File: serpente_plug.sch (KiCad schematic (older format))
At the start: 26 parts, among them J1 USB_A, J2 Conn_Power, J3 Conn_GPIO, SW1 SW_RESET, U1 GD25Q32CNIGR, U2 MCP1700-3302E_SOT23, U3 ATSAMD21E18A

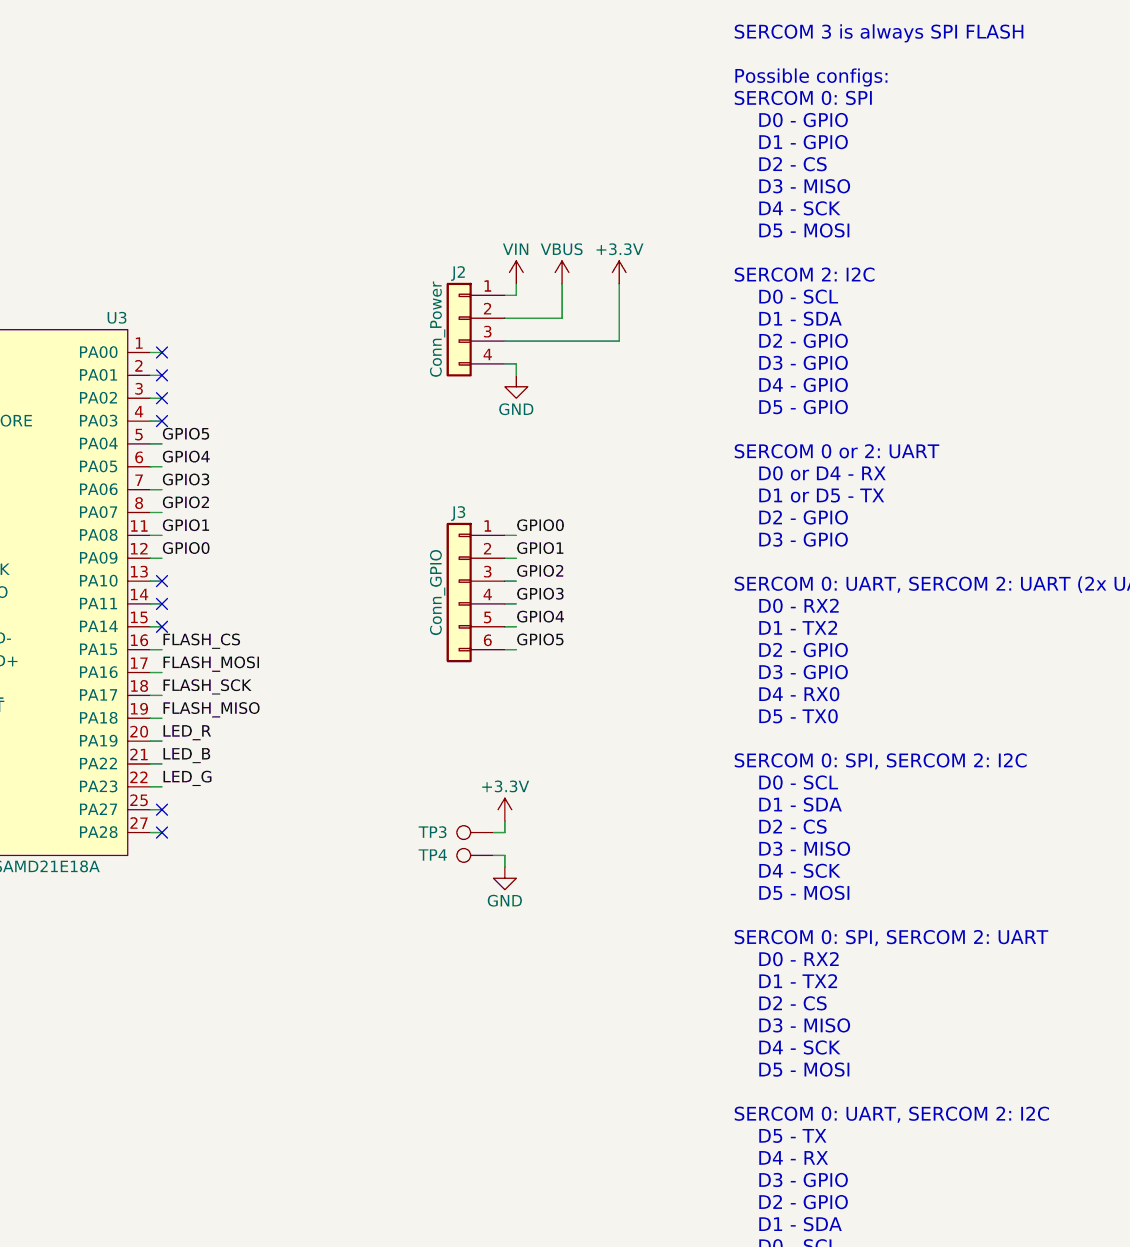
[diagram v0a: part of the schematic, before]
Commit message: Fix GPIO numbers, add BOM, update README
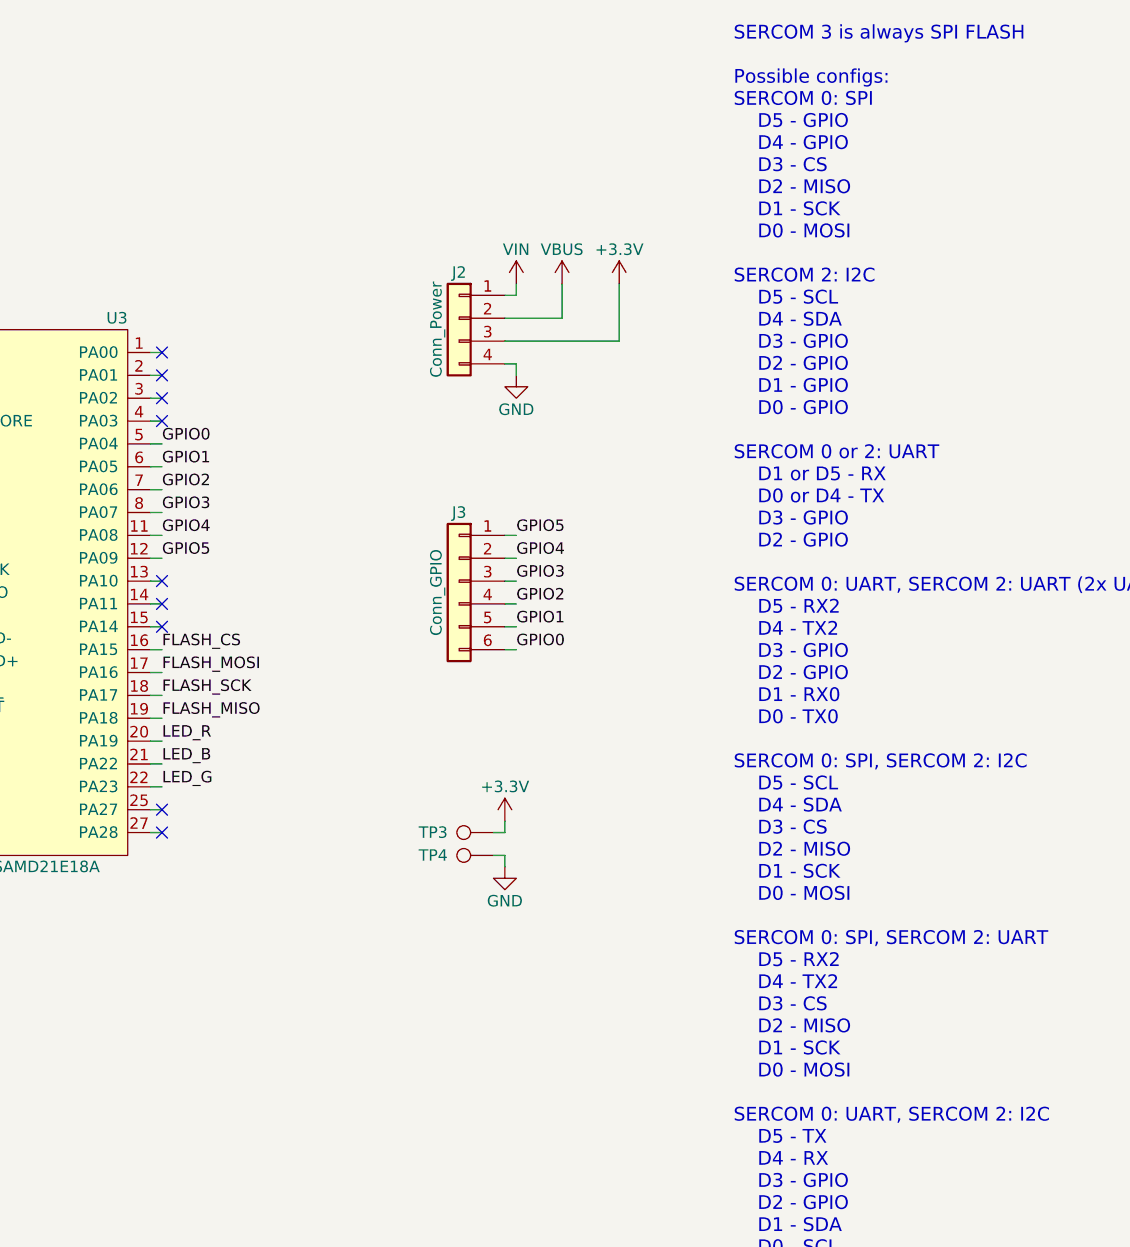
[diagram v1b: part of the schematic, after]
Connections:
- net GPIO0: now also J3.6 (Pin_6), U3.5 (PA04); no longer J3.1 (Pin_1), U3.12 (PA09)
- net GPIO1: now also J3.5 (Pin_5), U3.6 (PA05); no longer J3.2 (Pin_2), U3.11 (PA08)
- net GPIO2: now also J3.4 (Pin_4), U3.7 (PA06); no longer J3.3 (Pin_3), U3.8 (PA07)
- net GPIO3: now also J3.3 (Pin_3), U3.8 (PA07); no longer J3.4 (Pin_4), U3.7 (PA06)
- net GPIO4: now also J3.2 (Pin_2), U3.11 (PA08); no longer J3.5 (Pin_5), U3.6 (PA05)
- net GPIO5: now also J3.1 (Pin_1), U3.12 (PA09); no longer J3.6 (Pin_6), U3.5 (PA04)
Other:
- note added: "SERCOM 3 is always SPI FLASH\n\nPossible configs:\nSERCOM 0: SPI\n D5 - GPIO\n D4 - GPIO\n D3 - CS\n D2 - MISO\n D1 - SCK\n D0 - MOSI\n \nSERCOM 2: I2C\n D5 - SCL\n D4 - SDA\n D3 - GPIO\n D2 - GPIO\n D1 - GPIO\n D0 - GPIO\n\nSERCOM 0 or 2: UART\n D1 or D5 - RX\n D0 or D4 - TX\n D3 - GPIO\n D2 - GPIO\n\nSERCOM 0: UART, SERCOM 2: UART (2x UART)\n D5 - RX2\n D4 - TX2\n D3 - GPIO\n D2 - GPIO\n D1 - R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"
- note removed: "SERCOM 3 is always SPI FLASH\n\nPossible configs:\nSERCOM 0: SPI\n D0 - GPIO\n D1 - GPIO\n D2 - CS\n D3 - MISO\n D4 - SCK\n D5 - MOSI\n \nSERCOM 2: I2C\n D0 - SCL\n D1 - SDA\n D2 - GPIO\n D3 - GPIO\n D4 - GPIO\n D5 - GPIO\n\nSERCOM 0 or 2: UART\n D0 or D4 - RX\n D1 or D5 - TX\n D2 - GPIO\n D3 - GPIO\n\nSERCOM 0: UART, SERCOM 2: UART (2x UART)\n D0 - RX2\n D1 - TX2\n D2 - GPIO\n D3 - GPIO\n D4 - R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"
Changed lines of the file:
@@
 EESchema Schematic File Version 4
+LIBS:serpente_plug-cache
 EELAYER 29 0
 EELAYER END
@@
 Text Label 6350 3900 0    50   ~ 0
 LED_B
+Text Label 7900 3400 0    50   ~ 0
+GPIO0
+Text Label 7900 3300 0    50   ~ 0
+GPIO1
+Text Label 7900 3200 0    50   ~ 0
+GPIO2
+Text Label 7900 3100 0    50   ~ 0
+GPIO3
+Text Label 7900 3000 0    50   ~ 0
+GPIO4
 Text Label 7900 2900 0    50   ~ 0
+GPIO5
+Text Label 6350 2500 0    50   ~ 0
 GPIO0
-Text Label 7900 3000 0    50   ~ 0
+Text Label 6350 2600 0    50   ~ 0
 GPIO1
-Text Label 7900 3100 0    50   ~ 0
+Text Label 6350 2700 0    50   ~ 0
 GPIO2
-Text Label 7900 3200 0    50   ~ 0
+Text Label 6350 2800 0    50   ~ 0
 GPIO3
-Text Label 7900 3300 0    50   ~ 0
+Text Label 6350 2900 0    50   ~ 0
 GPIO4
-Text Label 7900 3400 0    50   ~ 0
-GPIO5
 Text Label 6350 3000 0    50   ~ 0
-GPIO0
-Text Label 6350 2900 0    50   ~ 0
-GPIO1
-Text Label 6350 2800 0    50   ~ 0
-GPIO2
-Text Label 6350 2700 0    50   ~ 0
-GPIO3
-Text Label 6350 2600 0    50   ~ 0
-GPIO4
-Text Label 6350 2500 0    50   ~ 0
 GPIO5
 Text Label 4750 3350 2    50   ~ 0
@@
 FLASH_MISO
 Text Notes 8850 6250 0    60   ~ 0
-SERCOM 3 is always SPI FLASH\n\nPossible configs:\nSERCOM 0: SPI\n    D0 - GPIO\n    D1 - GPIO\n    D2 - CS\n    D3 - MISO\n    D4 - SCK\n    D5 - MOSI\n    \nSERCOM 2: I2C\n    D0 - SCL\n    D1 - SDA\n    D2 - GPIO\n    D3 - GPIO\n    D4 - GPIO\n    D5 - GPIO\n\nSERCOM 0 or 2: UART\n    D0 or D4 - RX\n    D1 or D5 - TX\n    D2 - GPIO\n    D3 - GPIO\n\nSERCOM 0: UART, SERCOM 2: UART (2x UART)\n    D0 - RX2\n    D1 - TX2\n    D2 - GPIO\n    D3 - GPIO\n    D4 - RX0\n    D5 - TX0\n\nSERCOM 0: SPI, SERCOM 2: I2C\n    D0 - SCL\n    D1 - SDA\n    D2 - CS\n    D3 - MISO\n    D4 - SCK\n    D5 - MOSI\n\nSERCOM 0: SPI, SERCOM 2: UART\n    D0 - RX2\n    D1 - TX2\n    D2 - CS\n    D3 - MISO\n    D4 - SCK\n    D5 - MOSI\n\nSERCOM 0: UART, SERCOM 2: I2C\n    D5 - TX\n    D4 - RX\n    D3 - GPIO\n    D2 - GPIO\n    D1 - SDA\n    D0 - SCL\n\nAll GPIOs are PWM-enabled!\n
+SERCOM 3 is always SPI FLASH\n\nPossible configs:\nSERCOM 0: SPI\n    D5 - GPIO\n    D4 - GPIO\n    D3 - CS\n    D2 - MISO\n    D1 - SCK\n    D0 - MOSI\n    \nSERCOM 2: I2C\n    D5 - SCL\n    D4 - SDA\n    D3 - GPIO\n    D2 - GPIO\n    D1 - GPIO\n    D0 - GPIO\n\nSERCOM 0 or 2: UART\n    D1 or D5 - RX\n    D0 or D4 - TX\n    D3 - GPIO\n    D2 - GPIO\n\nSERCOM 0: UART, SERCOM 2: UART (2x UART)\n    D5 - RX2\n    D4 - TX2\n    D3 - GPIO\n    D2 - GPIO\n    D1 - RX0\n    D0 - TX0\n\nSERCOM 0: SPI, SERCOM 2: I2C\n    D5 - SCL\n    D4 - SDA\n    D3 - CS\n    D2 - MISO\n    D1 - SCK\n    D0 - MOSI\n\nSERCOM 0: SPI, SERCOM 2: UART\n    D5 - RX2\n    D4 - TX2\n    D3 - CS\n    D2 - MISO\n    D1 - SCK\n    D0 - MOSI\n\nSERCOM 0: UART, SERCOM 2: I2C\n    D5 - TX\n    D4 - RX\n    D3 - GPIO\n    D2 - GPIO\n    D1 - SDA\n    D0 - SCL\n\nAll GPIOs are PWM-enabled!
 NoConn ~ 6350 2100
 NoConn ~ 6350 2200

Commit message: Final rev 2 release!
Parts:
- removed R7, R8: 22R, Resistor_SMD:R_0603_1608Metric, symbol Device:R_Small
- added TP7: TP_RESET, TestPoint:TestPoint_Pad_D1.0mm, symbol Connector:TestPoint
- D3: value LED_ARGB -> LED_RBAG; symbol Device_Extra:LED_RBGA -> Device_Extra:LED_RBAG
- J2: footprint Connector_PinHeader_2.54mm:PinHeader_1x04_P2.54mm_Vertical -> Connector_PinHeader_2.54mm_Extra:PinHeader_1x04_P2.54mm_Vertical_Castellated
- J3: footprint Connector_PinHeader_2.54mm:PinHeader_1x06_P2.54mm_Vertical -> Connector_PinHeader_2.54mm_Extra:PinHeader_1x06_P2.54mm_Vertical_Castellated
- SW1: footprint Button_Switch_SMD:SW_SPST_B3U-1000P -> Button_Switch_SMD:SW_SPST_B3U-1000P-B
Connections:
- net +3V3: now also D3.3 (A), J2.4 (Pin_4); no longer D3.4 (A), J2.3 (Pin_3)
- net GND: now also J2.3 (Pin_3); no longer J2.4 (Pin_4)
- net LED_B: now also U3.22 (PA23); no longer U3.21 (PA22)
- net LED_G: now also U3.20 (PA19); no longer U3.22 (PA23)
- net LED_R: now also U3.21 (PA22); no longer U3.20 (PA19)
- net USB_D+: now also U3.24 (USB_D+)
- net USB_D-: now also U3.23 (USB_D-)
- net ~RESET~: now reaches SW1.2 (B), U3.26 (~RESET~)
- net ~RESET~: now also TP7.1
- net at R2.1: now also D3.4 (GK); no longer D3.3 (GK)
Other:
- moved on the sheet: SW1, TP4, TP5, TP6
